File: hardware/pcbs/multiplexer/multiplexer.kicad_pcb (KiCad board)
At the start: 2 copper layers, 19 parts, among them K1 CONN_3, K2 CONN_3, P1 CONN_5X2, P2 CONN_5X2, P3 CONN_2, P4 CONN_2, P5 CONN_7, U1 ADG44X, U2 ADG44X, U3 ADG44X, U4 ADG44X

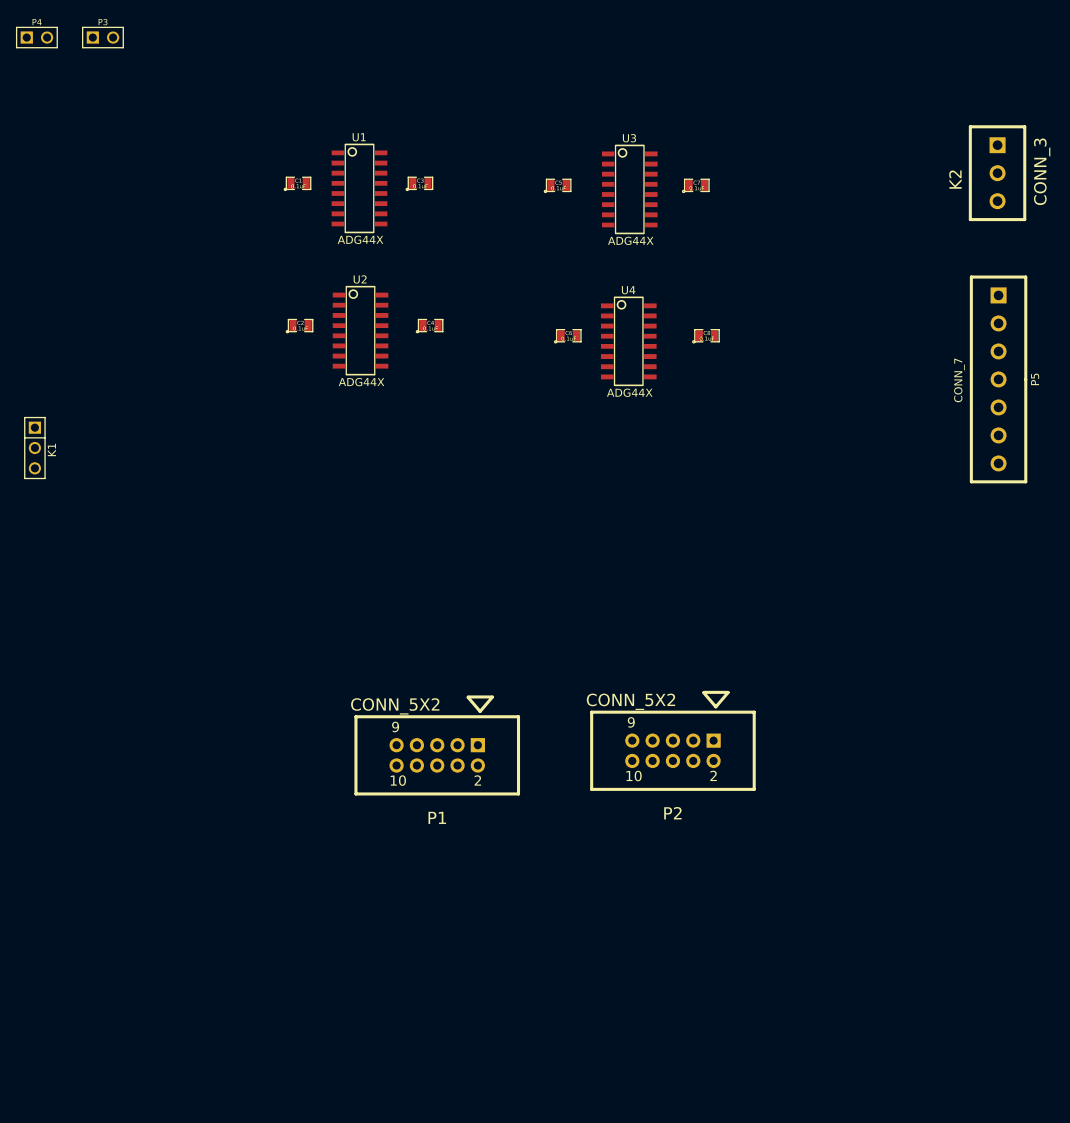
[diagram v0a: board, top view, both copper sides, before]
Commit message: Finished initial layout and routing of make-before-break multiplexer expansion board.
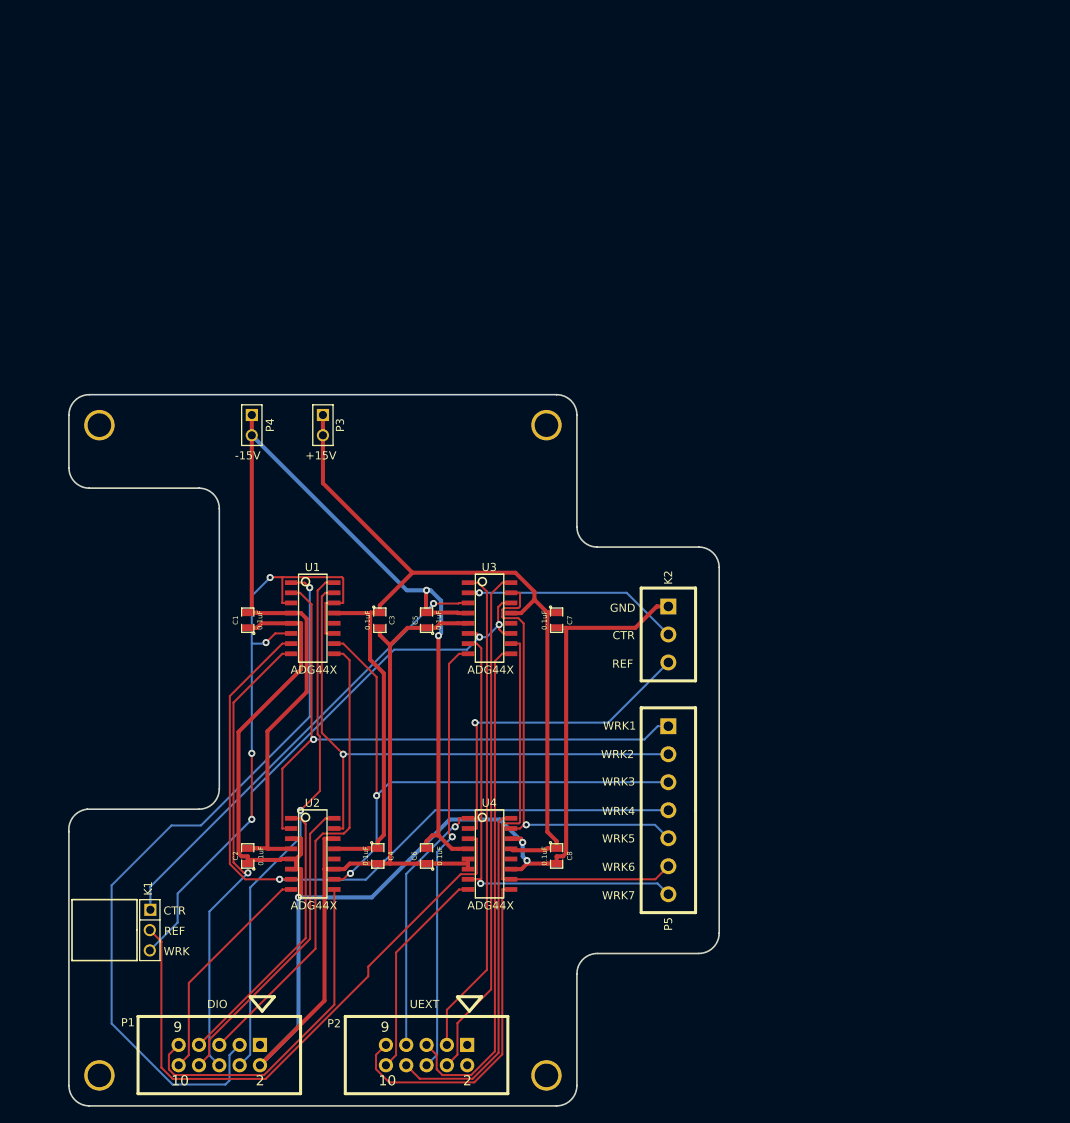
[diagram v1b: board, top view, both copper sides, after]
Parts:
- added 4-40: VAL**, 4-40, F.Cu at (80.0, 161.3)
- added M1: VAL**, 4-40, F.Cu at (80.0, 80.0)
- added M2: VAL**, 4-40, F.Cu at (135.9, 80.0)
- added M3: VAL**, 4-40, F.Cu at (135.9, 161.3)
- moved K2 70.8 mm to (151.1, 106.2)
- moved P5 67.8 mm to (151.1, 128.1)
- moved C8 67.7 mm to (137.2, 133.9), turned to 270 degrees
- moved C6 67.4 mm to (120.9, 133.9), turned to 90 degrees
- moved C2 66.6 mm to (98.6, 133.9), turned to 90 degrees
- moved C4 66.6 mm to (114.8, 133.9), turned to 270 degrees
- moved U4 66.4 mm to (128.8, 133.6)
- moved U2 65.7 mm to (106.7, 133.6)
- moved K1 61.9 mm to (86.3, 143.1)
- moved C7 57.1 mm to (137.2, 104.4), turned to 270 degrees
- moved C5 56.8 mm to (120.9, 104.4), turned to 90 degrees
- moved U3 56.4 mm to (128.8, 104.1)
- moved P3 55.7 mm to (108.0, 80.0), turned to 270 degrees
- moved P4 55.4 mm to (99.1, 80.0), turned to 270 degrees
- moved C1 55.0 mm to (98.6, 104.4), turned to 90 degrees
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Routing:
- net /GND: track 0.00 -> 263.0 mm, vias 0 -> 3
- net /-15V: track 0.00 -> 145.4 mm, vias 0 -> 2
- net /WRK: track 0.00 -> 133.1 mm, vias 0 -> 6
- net /+15V: track 0.00 -> 132.7 mm
- net /D24: track 0.00 -> 92.6 mm, vias 0 -> 1
- net /WRK_4: track 0.00 -> 92.0 mm, vias 0 -> 1
- net /WRK_1: track 0.00 -> 79.1 mm, vias 0 -> 1
- net /REF: track 0.00 -> 74.6 mm
- net /WRK_2: track 0.00 -> 73.6 mm, vias 0 -> 1
- net /WRK_3: track 0.00 -> 72.4 mm, vias 0 -> 2
- net /D25: track 0.00 -> 66.1 mm, vias 0 -> 1
- net /D4: track 0.00 -> 64.3 mm
- net /D19: track 0.00 -> 63.6 mm
- net /D3: track 0.00 -> 61.6 mm
- net /D27: track 0.00 -> 58.6 mm, vias 0 -> 1
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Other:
- board outline added: 81.3 x 88.9 mm
- net class Default: clearance 0.254 -> 0.2032
- net class Power added: clearance 0.2032, trace_width 0.508, via_dia 0.889, via_drill 0.635
- rule trace_clearance: 0.254 -> 0.2032
- board text added: "+15V"
- board text added: "-15V"
- board text added: "CTR"
- board text added: "DIO"
- board text added: "GND"
- board text added: "REF"
- board text added: "UEXT"
- board text added: "WRK"
- board text added: "WRK1"
- board text added: "WRK2"
- board text added: "WRK3"
- board text added: "WRK4"
- board text added: "WRK5"
- board text added: "WRK6"
- board text added: "WRK7"

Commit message: Added BOM.txt and gerber files.
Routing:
- net /GND: track 263.0 -> 294.6 mm
- net /D3: track 61.6 -> 91.8 mm
- net /D24: track 92.6 -> 62.8 mm, vias 1 -> 0
- net /REF: track 74.6 -> 45.2 mm, vias 0 -> 1
- net /+15V: track 132.7 -> 161.5 mm
- net /WRK: track 133.1 -> 105.4 mm, vias 6 -> 2
- net /D13: track 43.2 -> 67.2 mm
- net /D25: track 66.1 -> 86.0 mm
- net /-15V: track 145.4 -> 130.7 mm, vias 2 -> 4
- net /WRK_4: track 92.0 -> 77.6 mm, vias 1 -> 2
- net /D30: track 42.6 -> 28.2 mm, vias 0 -> 1
- net /D18: track 54.6 -> 65.2 mm, vias 1 -> 0
- net /D26: track 58.6 -> 68.9 mm, vias 0 -> 1
- net /D19: track 63.6 -> 54.0 mm, vias 0 -> 1
- net /D27: track 58.6 -> 66.3 mm, vias 1 -> 0
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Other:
- net class Default: trace_width 0.254 -> 0.381
- net class Power: trace_width 0.508 -> 0.381
- board text added: "Rodeostat Multiplexer V0.1 R1 IO Rodeo Inc. www.iorodeo.com"

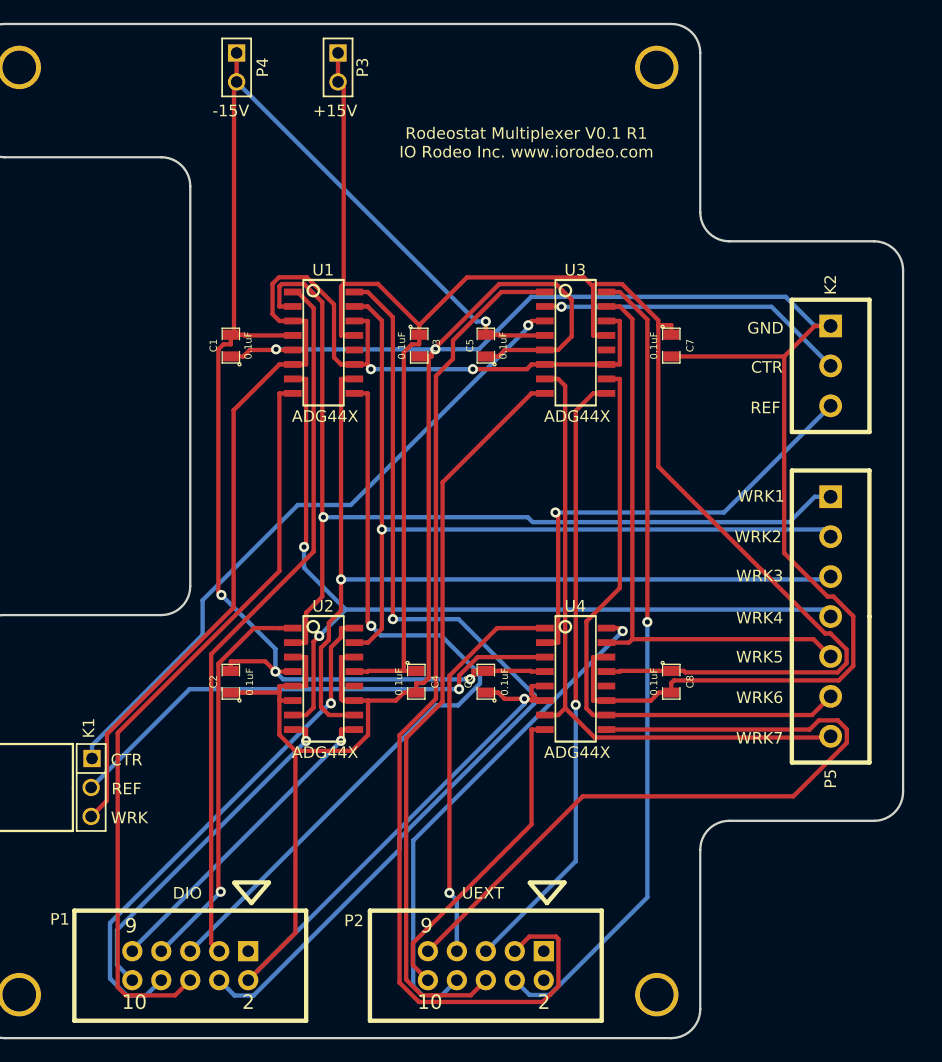
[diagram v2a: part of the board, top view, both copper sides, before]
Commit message: Renamed multiplexer directories.
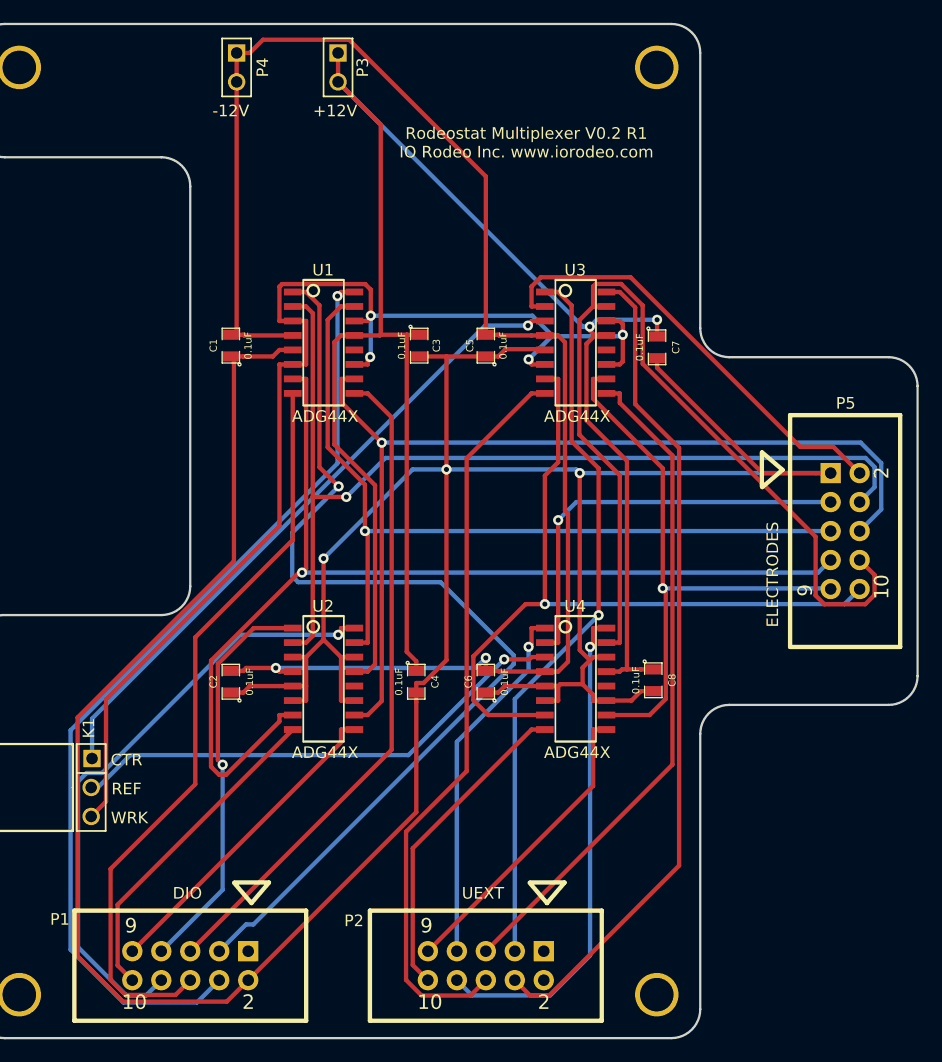
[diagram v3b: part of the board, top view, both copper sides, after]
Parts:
- removed K2: CONN_3, CONNBLOCK3
- P5: value CONN_7 -> CONN_5X2; footprint CONNBLOCK7 -> 5X2_SHRD_HEADER
- moved P5 7.60 mm to (152.4, 120.7)
- moved C8 1.58 mm to (135.6, 133.7)
- moved C7 1.25 mm to (135.9, 104.5)
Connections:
- net /+15V renamed /+12V
- net /-15V renamed /-12V
- P5 pad 1: /WRK_1 -> /GND
- P5 pad 2: /WRK_2 -> /CTR_SW
- P5 pad 3: /WRK_3 -> /REF_SW
- P5 pad 4: /WRK_4 -> /WRK_1
- P5 pad 5: /WRK_5 -> /WRK_2
- P5 pad 6: /WRK_6 -> /WRK_3
- P5 pad 7: /WRK_7 -> /WRK_4
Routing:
- net /D13: track 67.2 -> 26.6 mm
- net /WRK_5: track 51.2 -> 81.9 mm
- net /D3: track 91.8 -> 63.5 mm, vias 0 -> 1
- net /D24: track 62.8 -> 88.3 mm, vias 0 -> 1
- net /WRK_4: track 77.6 -> 95.5 mm, vias 2 -> 1
- net /CTR_SW: track 27.2 -> 39.1 mm, vias 1 -> 0
- net /WRK_7: track 56.7 -> 68.3 mm, vias 0 -> 1
- net /D26: track 68.9 -> 58.2 mm, vias 1 -> 0
- net /+12V: track 161.5 -> 171.3 mm, vias 0 -> 2
- net /-12V: track 130.7 -> 139.8 mm, vias 4 -> 2
- net /WRK_3: track 76.9 -> 85.1 mm
- net /D29: track 46.0 -> 54.1 mm
- net /D19: track 54.0 -> 58.8 mm, vias 1 -> 0
- net /WRK: track 105.4 -> 109.7 mm, vias 2 -> 4
- net /REF_SW: track 40.7 -> 36.4 mm
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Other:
- board size 81.3 x 88.9 mm -> 82.6 x 88.9 mm
- board text added: "+12V"
- board text added: "-12V"
- board text added: "ELECTRODES"
- board text added: "Rodeostat Multiplexer V0.2 R1 IO Rodeo Inc. www.iorodeo.com"
- board text removed: "+15V"
- board text removed: "-15V"
- board text removed: "GND"
- board text removed: "Rodeostat Multiplexer V0.1 R1 IO Rodeo Inc. www.iorodeo.com"
- board text removed: "WRK1"
- board text removed: "WRK2"
- board text removed: "WRK3"
- board text removed: "WRK4"
- board text removed: "WRK5"
- board text removed: "WRK6"
- board text removed: "WRK7"
